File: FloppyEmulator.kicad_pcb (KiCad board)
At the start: 2 copper layers, 69.9 x 48.3 mm, 52 parts, among them Q1 Crystal_GND24, Q2 BC817, Q3 BC817, SW1 ALPS_5WAY, U1 STM32F405RGTx, U10 AP1117-15, U2 SN74LVC2G07, U3 SN74LVC2G07, U4 SN74LVC2G07, U5 SN74LVC2G07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

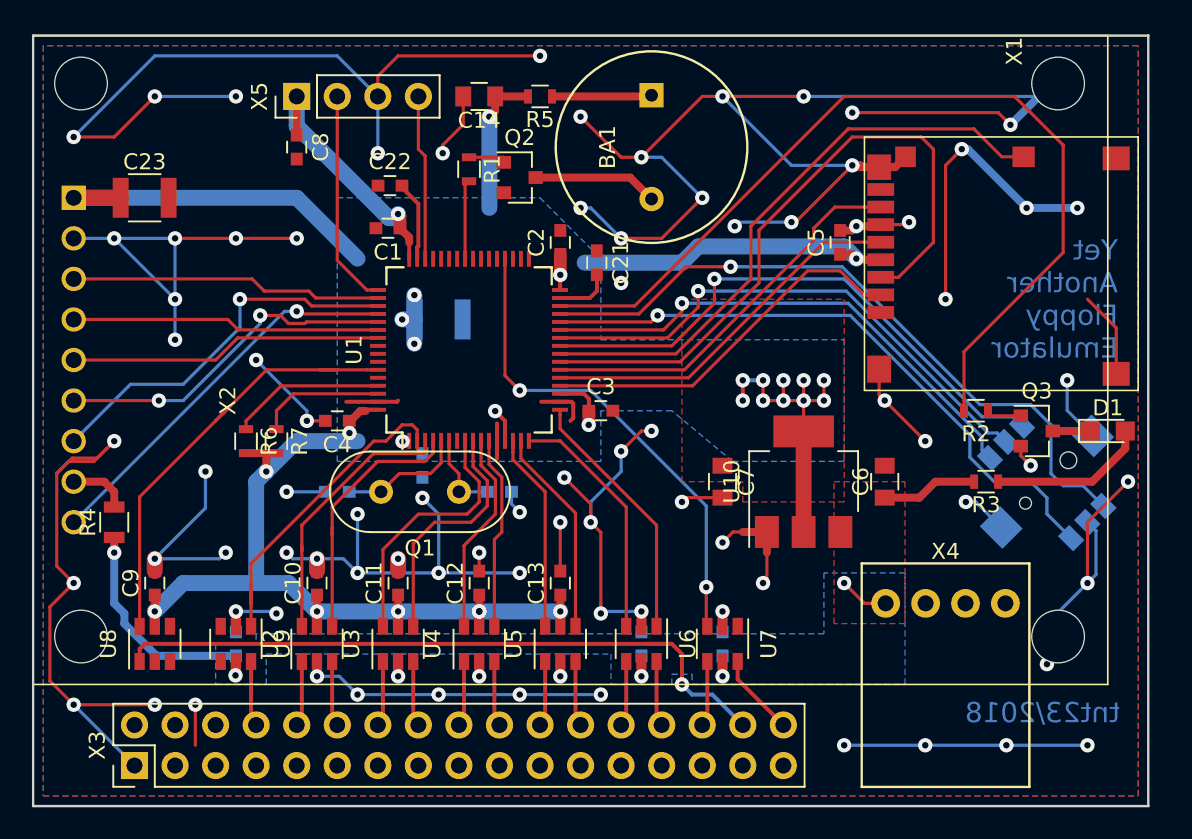
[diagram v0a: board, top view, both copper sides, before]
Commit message: PCB trimmed to updated LCD shield
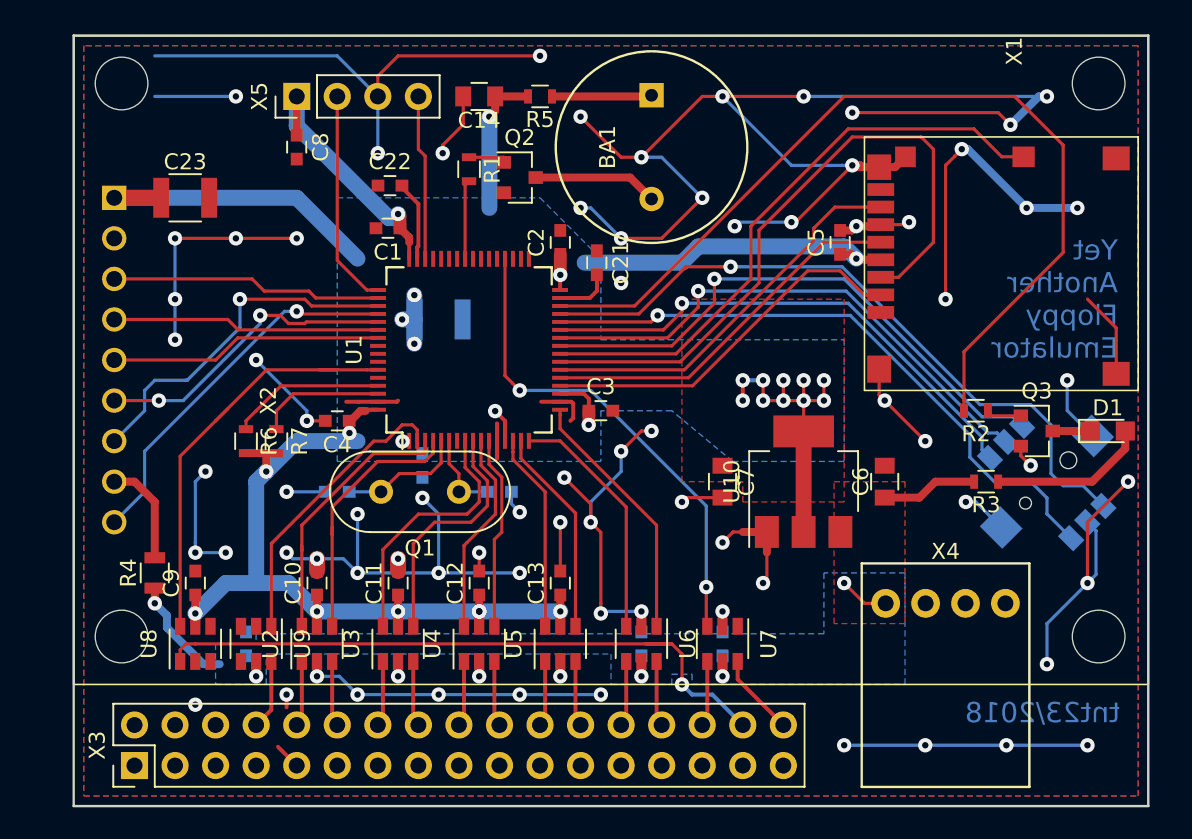
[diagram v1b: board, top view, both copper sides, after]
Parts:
- moved R4 4.07 mm to (147.3, 90.8)
- moved C9 2.54 mm to (149.9, 91.4)
- moved U8 2.54 mm to (149.9, 95.2)
- moved C23 2.54 mm to (149.2, 67.3)
- moved X2 2.54 mm to (144.8, 77.5)
- moved U9 1.27 mm to (153.7, 95.2)
- moved C16 0.63 mm to (153.0, 95.2)
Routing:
- net GND: track 397.1 -> 329.9 mm, vias 88 -> 81
- net +5VDC: track 29.2 -> 21.5 mm
- net +3V3: track 153.4 -> 146.9 mm
- net /BACKLIGHT: track 3.76 -> 6.56 mm
- net Net-(U8-Pad1): track 43.6 -> 41.0 mm
- net SPI3_NSS: track 19.6 -> 17.0 mm
- net SPI3_MOSI: track 21.8 -> 19.3 mm
- net /LCD_RESET: track 19.3 -> 16.8 mm
- net /LCD_DC: track 19.6 -> 17.1 mm
- net /INDEX: track 20.0 -> 18.2 mm
- net (no net): track 2.54 -> 1.09 mm
- net SPI3_MISO: track 24.6 -> 23.6 mm
- net /SIDE: track 28.5 -> 27.5 mm
- net SPI3_SCK: track 24.0 -> 22.9 mm, vias 1 -> 2
- net Net-(U9-Pad6): track 4.11 -> 4.83 mm
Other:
- board size 69.9 x 48.3 mm -> 67.3 x 48.3 mm

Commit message: Copper cleanup
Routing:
- net GND: track 329.9 -> 342.3 mm, vias 81 -> 84
- net SPI3_SCK: track 22.9 -> 22.3 mm, vias 2 -> 1

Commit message: More cleanups
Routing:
- net (no net): track 1.09 -> 0.00 mm
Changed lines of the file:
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@@
     (thickness 1.6)
     (drawings 10)
-    (tracks 662)
+    (tracks 660)
     (zones 0)
     (modules 52)
@@
   (segment (start 172.72 96.35) (end 172.72 97.282) (width 0.5) (layer F.Cu) (net 8))
   (via (at 172.72 97.282) (size 0.9) (drill 0.4) (layers F.Cu B.Cu) (net 8))
+  (segment (start 177.8 71.374) (end 178.816 70.358) (width 1) (layer B.Cu) (net 9))
+  (segment (start 174.244 71.374) (end 177.8 71.374) (width 1) (layer B.Cu) (net 9))
+  (segment (start 190.5 70.358) (end 191.262 71.12) (width 1) (layer B.Cu) (net 9))
+  (segment (start 178.816 70.358) (end 190.5 70.358) (width 1) (layer B.Cu) (net 9))
   (segment (start 149.86 94.15) (end 149.86 93.345) (width 0.5) (layer F.Cu) (net 9))
   (segment (start 147.725 67.31) (end 144.78 67.31) (width 1) (layer F.Cu) (net 9))
@@
   (segment (start 163.255 82.535) (end 162.873662 82.535) (width 0.25) (layer F.Cu) (net 9))
   (via (at 162.836331 82.572331) (size 0.9) (drill 0.4) (layers F.Cu B.Cu) (net 9))
-  (segment (start 180.34 71.374) (end 181.356 70.358) (width 1) (layer B.Cu) (net 9))
-  (segment (start 190.5 70.358) (end 191.262 71.12) (width 1) (layer B.Cu) (net 9))
-  (segment (start 174.244 71.374) (end 180.34 71.374) (width 1) (layer B.Cu) (net 9))
-  (segment (start 181.356 70.358) (end 190.5 70.358) (width 1) (layer B.Cu) (net 9))
   (segment (start 168.275 62.23) (end 168.275 67.945) (width 1) (layer B.Cu) (net 9))
   (segment (start 168.64 61.865) (end 168.275 62.23) (width 0.5) (layer F.Cu) (net 9))
@@
   (segment (start 165.255 82.535) (end 165.255 83.919) (width 0.2) (layer F.Cu) (net 66))
   (via (at 180.34 97.790008) (size 0.9) (drill 0.4) (layers F.Cu B.Cu) (net 69))
-  (segment (start 146.37 95.57) (end 146.69 95.25) (width 0.25) (layer F.Cu) (net 0))
   (segment (start 153.35 100.01) (end 153.67 100.33) (width 0.25) (layer F.Cu) (net 70))
   (segment (start 181.356 74.168) (end 181.356 73.152) (width 0.2) (layer F.Cu) (net 75))
@@
   (segment (start 172.705 74.085) (end 177.375 74.085) (width 0.2) (layer F.Cu) (net 83))
   (segment (start 177.375 74.085) (end 190.5 60.96) (width 0.2) (layer F.Cu) (net 83))
-  (segment (start 145.415 93.345) (end 145.415 93.98) (width 0.5) (layer B.Cu) (net 0))
   (segment (start 150.368 96.52) (end 151.384 96.52) (width 0.5) (layer B.Cu) (net 84))
   (segment (start 148.082 94.234) (end 150.368 96.52) (width 0.5) (layer B.Cu) (net 84))

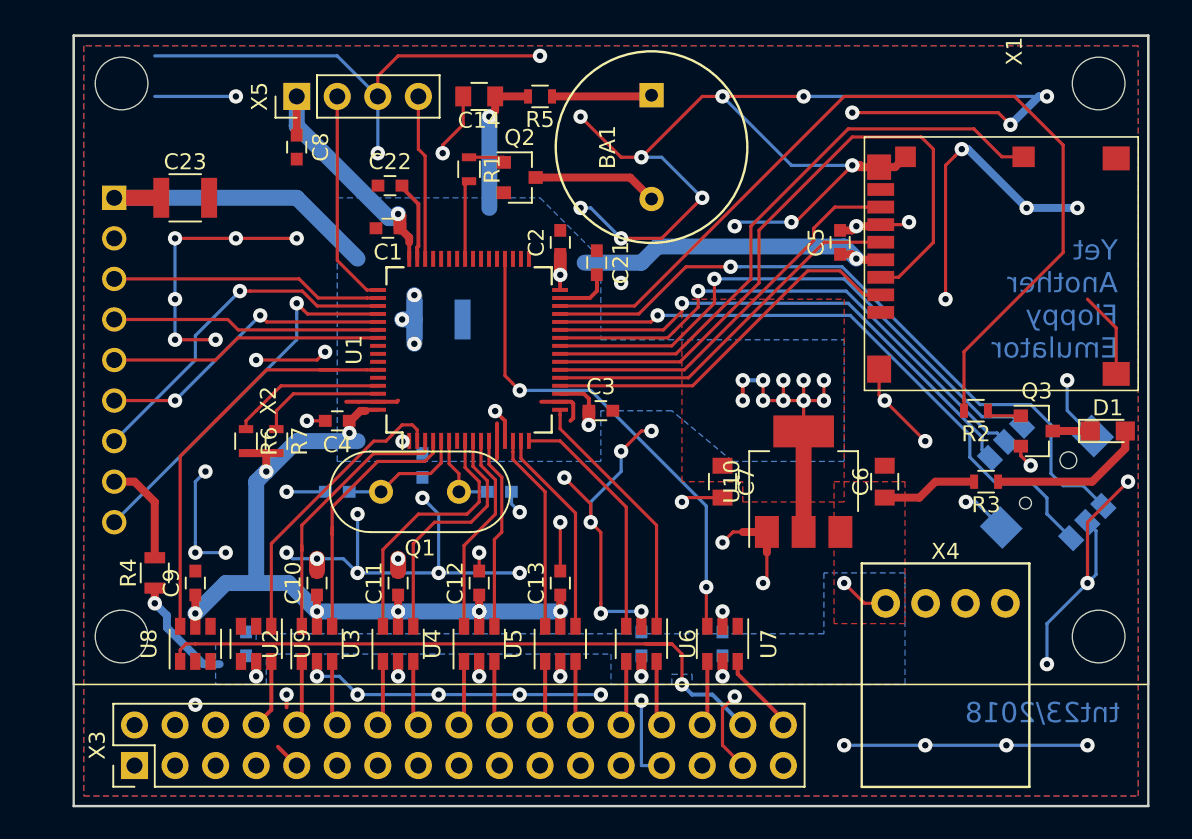
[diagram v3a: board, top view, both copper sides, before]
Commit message: Fixed LCD shield dimensions
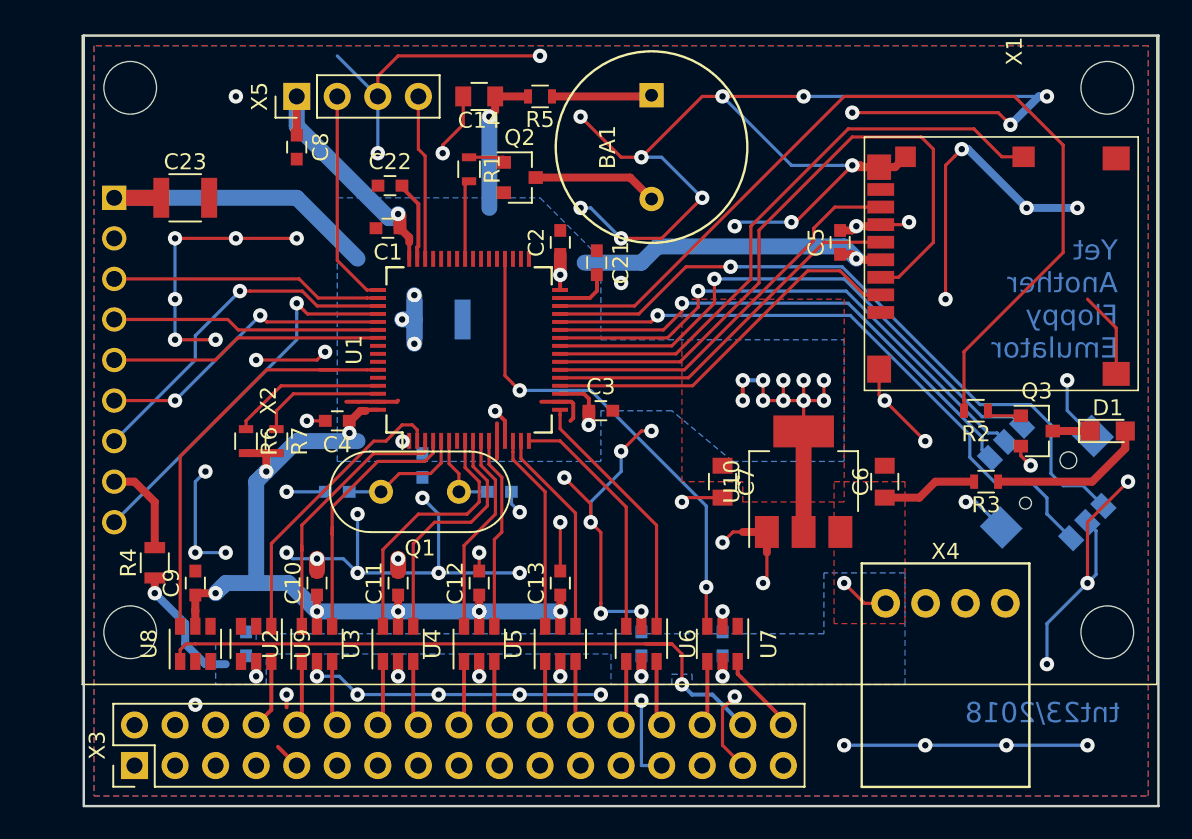
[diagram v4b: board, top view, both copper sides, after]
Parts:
- X2: footprint components:QVGA_LCD_9pin -> QVGA_LCD_9pin
- moved R4 0.64 mm to (147.3, 90.2)
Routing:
- net GND: track 342.3 -> 325.8 mm, vias 84 -> 83
- net +5VDC: track 21.5 -> 22.5 mm
- net /BACKLIGHT: track 6.56 -> 5.93 mm
- net (no net): vias 1 -> 2

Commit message: PCB size adjusted
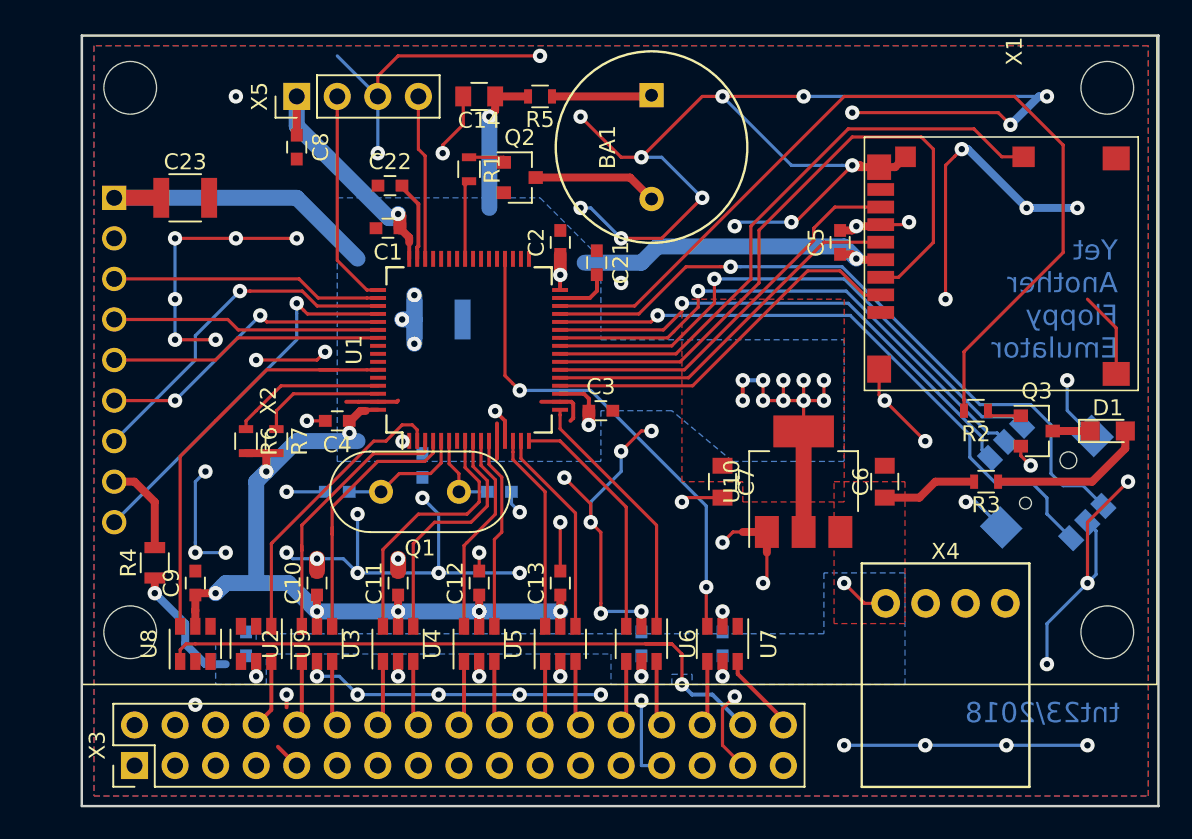
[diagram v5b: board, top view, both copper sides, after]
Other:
- board size 67.3 x 48.3 mm -> 67.4 x 48.3 mm
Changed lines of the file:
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@@
     (arrow2b (pts (xy 216.535 57.15) (xy 217.121421 58.276504)))
   )
-  (dimension 67.31 (width 0.3) (layer F.SilkS)
-    (gr_text "67.310 mm" (at 176.53 115.65) (layer F.SilkS)
+  (dimension 67.437 (width 0.3) (layer F.SilkS)
+    (gr_text "67.437 mm" (at 176.4665 115.65) (layer F.SilkS)
       (effects (font (size 1.5 1.5) (thickness 0.3)))
     )
     (feature1 (pts (xy 210.185 105.41) (xy 210.185 117)))
-    (feature2 (pts (xy 142.875 105.41) (xy 142.875 117)))
-    (crossbar (pts (xy 142.875 114.3) (xy 210.185 114.3)))
+    (feature2 (pts (xy 142.748 105.41) (xy 142.748 117)))
+    (crossbar (pts (xy 142.748 114.3) (xy 210.185 114.3)))
     (arrow1a (pts (xy 210.185 114.3) (xy 209.058496 114.886421)))
     (arrow1b (pts (xy 210.185 114.3) (xy 209.058496 113.713579)))
-    (arrow2a (pts (xy 142.875 114.3) (xy 144.001504 114.886421)))
-    (arrow2b (pts (xy 142.875 114.3) (xy 144.001504 113.713579)))
+    (arrow2a (pts (xy 142.748 114.3) (xy 143.874504 114.886421)))
+    (arrow2b (pts (xy 142.748 114.3) (xy 143.874504 113.713579)))
   )
   (gr_line (start 210.185 57.15) (end 210.185 105.41) (layer Edge.Cuts) (width 0.15))
-  (gr_line (start 142.875 57.15) (end 210.185 57.15) (layer Edge.Cuts) (width 0.15))
-  (gr_line (start 142.875 105.41) (end 142.875 57.15) (layer Edge.Cuts) (width 0.15))
-  (gr_line (start 210.185 105.41) (end 142.875 105.41) (layer Edge.Cuts) (width 0.15))
+  (gr_line (start 142.748 57.15) (end 210.185 57.15) (layer Edge.Cuts) (width 0.15))
+  (gr_line (start 142.748 105.41) (end 142.748 57.15) (layer Edge.Cuts) (width 0.15))
+  (gr_line (start 210.185 105.41) (end 142.748 105.41) (layer Edge.Cuts) (width 0.15))
   (via (at 149.86 99.06) (size 0.9) (drill 0.4) (layers F.Cu B.Cu) (net 0))
   (segment (start 156.210002 74.550396) (end 156.210002 73.914) (width 0.2) (layer B.Cu) (net 1))
